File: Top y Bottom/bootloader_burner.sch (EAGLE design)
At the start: 9 parts, among them J1 ZIFSOCKET-28-3", Y1 16MHz

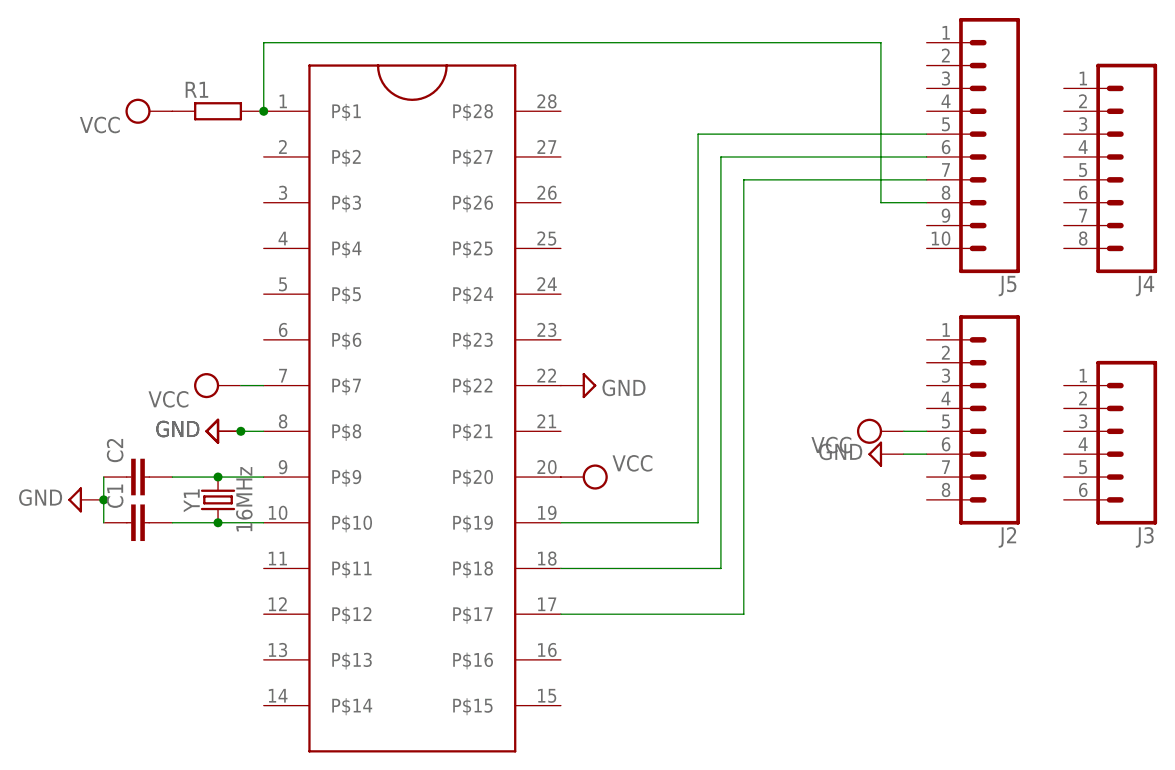
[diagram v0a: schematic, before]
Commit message: Cambie el diseño de la plaqueta con zif socket grande para que queden ordenados los pines con los del Arduino. Tambien cambie el dieño de la plaqueta doble (que igual hay que cambiarla poque la gracia de esa es que quede montada en el Arduino)
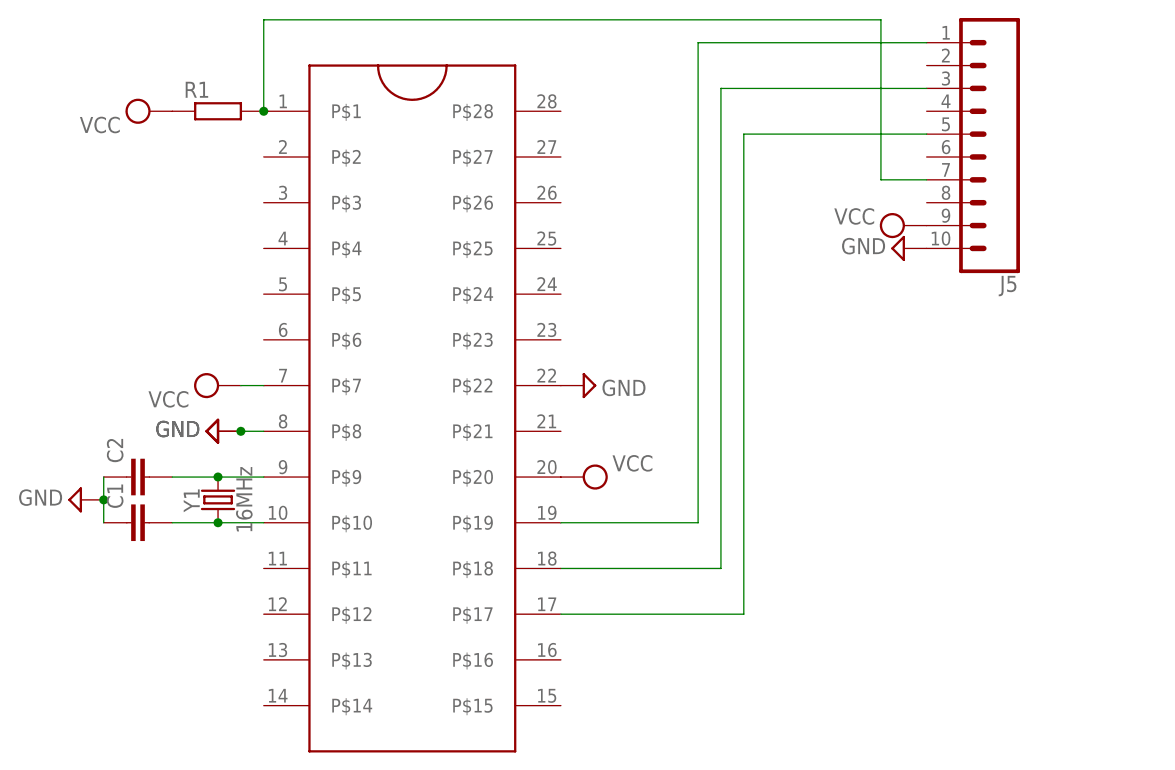
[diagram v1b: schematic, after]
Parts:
- removed J2, J4: (no value), SparkFun-Connectors:CONN_08"
- removed J3: (no value), SparkFun-Connectors:CONN_06SILK_FEMALE_PTH
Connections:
- removed net N$1: J1.P$17, J5.7
- removed net N$2: J1.P$18, J5.6
- removed net N$3: J1.P$19, J5.5
- removed net N$6: J1.P$1, J5.8, R1.2
- new net PIN_10: J1.P$1, J5.7, R1.2
- new net PIN_11: J1.P$17, J5.5
- new net PIN_12: J1.P$18, J5.3
- new net PIN_13: J1.P$19, J5.1
- net GND: now also J5.10; no longer J2.6
- net VCC: now also J5.9; no longer J2.5
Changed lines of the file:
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@@
 <part name="SUPPLY9" library="supply2" library_urn="urn:adsk.eagle:library:372" deviceset="GND" device=""/>
 <part name="R1" library="rcl" deviceset="R-EU_" device="0207/10" package3d_urn="urn:adsk.eagle:package:23491/2"/>
-<part name="J4" library="SparkFun-Connectors" deviceset="CONN_08" device="&quot;" package3d_urn="urn:adsk.eagle:package:38138/1"/>
 <part name="J5" library="SparkFun-Connectors" deviceset="CONN_10" device="&quot;" package3d_urn="urn:adsk.eagle:package:38157/1"/>
-<part name="J2" library="SparkFun-Connectors" deviceset="CONN_08" device="&quot;" package3d_urn="urn:adsk.eagle:package:38138/1"/>
-<part name="J3" library="SparkFun-Connectors" deviceset="CONN_06" device="SILK_FEMALE_PTH" package3d_urn="urn:adsk.eagle:package:38009/1"/>
 <part name="FRAME1" library="frames" library_urn="urn:adsk.eagle:library:229" deviceset="DINA4_L" device=""/>
 </parts>
@@
 <attribute name="VALUE" x="22.225" y="75.565" size="1.778" layer="96" rot="R180"/>
 </instance>
-<instance part="SUPPLY6" gate="G$1" x="106.68" y="40.64" smashed="yes" rot="R90">
-<attribute name="VALUE" x="103.505" y="40.005" size="1.778" layer="96" rot="R180"/>
+<instance part="SUPPLY6" gate="G$1" x="109.22" y="63.5" smashed="yes" rot="R90">
+<attribute name="VALUE" x="106.045" y="65.405" size="1.778" layer="96" rot="R180"/>
 </instance>
-<instance part="SUPPLY7" gate="GND" x="106.68" y="38.1" smashed="yes" rot="R270">
-<attribute name="VALUE" x="99.695" y="37.465" size="1.778" layer="96"/>
+<instance part="SUPPLY7" gate="GND" x="109.22" y="60.96" smashed="yes" rot="R270">
+<attribute name="VALUE" x="102.235" y="60.325" size="1.778" layer="96"/>
 </instance>
 <instance part="Y1" gate="G$1" x="33.02" y="33.02" smashed="yes" rot="R90">
@@
 <attribute name="VALUE" x="29.21" y="72.898" size="1.778" layer="96"/>
 </instance>
-<instance part="J4" gate="G$1" x="132.08" y="71.12" smashed="yes" rot="R180">
-<attribute name="VALUE" x="137.16" y="83.566" size="1.778" layer="96" font="vector" rot="R180"/>
-<attribute name="NAME" x="137.16" y="57.912" size="1.778" layer="95" font="vector" rot="R180"/>
-</instance>
 <instance part="J5" gate="G$1" x="121.92" y="66.04" smashed="yes" rot="R180">
 <attribute name="VALUE" x="121.92" y="88.646" size="1.778" layer="96" font="vector" rot="R180"/>
 <attribute name="NAME" x="121.92" y="57.912" size="1.778" layer="95" font="vector" rot="R180"/>
-</instance>
-<instance part="J2" gate="G$1" x="116.84" y="43.18" smashed="yes" rot="R180">
-<attribute name="VALUE" x="121.92" y="55.626" size="1.778" layer="96" font="vector" rot="R180"/>
-<attribute name="NAME" x="121.92" y="29.972" size="1.778" layer="95" font="vector" rot="R180"/>
-</instance>
-<instance part="J3" gate="G$1" x="132.08" y="40.64" smashed="yes" rot="R180">
-<attribute name="VALUE" x="137.16" y="50.546" size="1.778" layer="96" font="vector" rot="R180"/>
-<attribute name="NAME" x="137.16" y="29.972" size="1.778" layer="95" font="vector" rot="R180"/>
 </instance>
 <instance part="FRAME1" gate="G$1" x="-60.96" y="-48.26" smashed="yes"/>
@@
 </segment>
 <segment>
+<pinref part="J5" gate="G$1" pin="9"/>
 <pinref part="SUPPLY6" gate="G$1" pin="VCC"/>
-<wire x1="109.22" y1="40.64" x2="111.76" y2="40.64" width="0.1524" layer="91"/>
-<pinref part="J2" gate="G$1" pin="5"/>
 </segment>
 </net>
@@
 </segment>
 <segment>
+<pinref part="J5" gate="G$1" pin="10"/>
 <pinref part="SUPPLY7" gate="GND" pin="GND"/>
-<wire x1="109.22" y1="38.1" x2="111.76" y2="38.1" width="0.1524" layer="91"/>
-<pinref part="J2" gate="G$1" pin="6"/>
 </segment>
 </net>
-<net name="N$1" class="0">
+<net name="PIN_11" class="0">
 <segment>
-<wire x1="91.44" y1="68.58" x2="91.44" y2="20.32" width="0.1524" layer="91"/>
+<wire x1="91.44" y1="73.66" x2="91.44" y2="20.32" width="0.1524" layer="91"/>
 <pinref part="J1" gate="G$1" pin="P$17"/>
 <wire x1="91.44" y1="20.32" x2="71.12" y2="20.32" width="0.1524" layer="91"/>
-<wire x1="91.44" y1="68.58" x2="111.76" y2="68.58" width="0.1524" layer="91"/>
-<pinref part="J5" gate="G$1" pin="7"/>
+<pinref part="J5" gate="G$1" pin="5"/>
+<wire x1="91.44" y1="73.66" x2="111.76" y2="73.66" width="0.1524" layer="91"/>
 </segment>
 </net>
-<net name="N$2" class="0">
+<net name="PIN_12" class="0">
 <segment>
 <pinref part="J1" gate="G$1" pin="P$18"/>
-<wire x1="88.9" y1="71.12" x2="88.9" y2="25.4" width="0.1524" layer="91"/>
+<wire x1="88.9" y1="78.74" x2="88.9" y2="25.4" width="0.1524" layer="91"/>
 <wire x1="88.9" y1="25.4" x2="71.12" y2="25.4" width="0.1524" layer="91"/>
-<wire x1="88.9" y1="71.12" x2="111.76" y2="71.12" width="0.1524" layer="91"/>
-<pinref part="J5" gate="G$1" pin="6"/>
+<pinref part="J5" gate="G$1" pin="3"/>
+<wire x1="88.9" y1="78.74" x2="111.76" y2="78.74" width="0.1524" layer="91"/>
 </segment>
 </net>
-<net name="N$3" class="0">
+<net name="PIN_13" class="0">
 <segment>
 <pinref part="J1" gate="G$1" pin="P$19"/>
-<wire x1="86.36" y1="73.66" x2="86.36" y2="30.48" width="0.1524" layer="91"/>
+<wire x1="86.36" y1="83.82" x2="86.36" y2="30.48" width="0.1524" layer="91"/>
 <wire x1="86.36" y1="30.48" x2="71.12" y2="30.48" width="0.1524" layer="91"/>
-<wire x1="86.36" y1="73.66" x2="111.76" y2="73.66" width="0.1524" layer="91"/>
-<pinref part="J5" gate="G$1" pin="5"/>
+<pinref part="J5" gate="G$1" pin="1"/>
+<wire x1="86.36" y1="83.82" x2="111.76" y2="83.82" width="0.1524" layer="91"/>
 </segment>
 </net>
@@
 </segment>
 </net>
-<net name="N$6" class="0">
+<net name="PIN_10" class="0">
 <segment>
 <pinref part="J1" gate="G$1" pin="P$1"/>
-<wire x1="38.1" y1="76.2" x2="38.1" y2="83.82" width="0.1524" layer="91"/>
-<wire x1="38.1" y1="83.82" x2="106.68" y2="83.82" width="0.1524" layer="91"/>
+<wire x1="38.1" y1="76.2" x2="38.1" y2="86.36" width="0.1524" layer="91"/>
+<wire x1="38.1" y1="86.36" x2="106.68" y2="86.36" width="0.1524" layer="91"/>
 <pinref part="R1" gate="G$1" pin="2"/>
 <junction x="38.1" y="76.2"/>
-<wire x1="106.68" y1="83.82" x2="106.68" y2="66.04" width="0.1524" layer="91"/>
-<wire x1="106.68" y1="66.04" x2="111.76" y2="66.04" width="0.1524" layer="91"/>
-<pinref part="J5" gate="G$1" pin="8"/>
+<pinref part="J5" gate="G$1" pin="7"/>
+<wire x1="106.68" y1="86.36" x2="106.68" y2="68.58" width="0.1524" layer="91"/>
+<wire x1="106.68" y1="68.58" x2="111.76" y2="68.58" width="0.1524" layer="91"/>
 </segment>
 </net>
